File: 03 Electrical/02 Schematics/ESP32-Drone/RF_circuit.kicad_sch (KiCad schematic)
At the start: 0 parts

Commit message: started placing the esp32 circuitry
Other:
- note added: "Determine the LoRA module that we will use"
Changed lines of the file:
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@@
 	(generator_version "9.0")
 	(paper "A4")
+	(text "Determine the LoRA module that we will use \n"
+		(exclude_from_sim no)
+		(at 51.308 48.768 0)
+		(effects
+			(font
+				(size 1.27 1.27)
+			)
+		)
+	)
 )

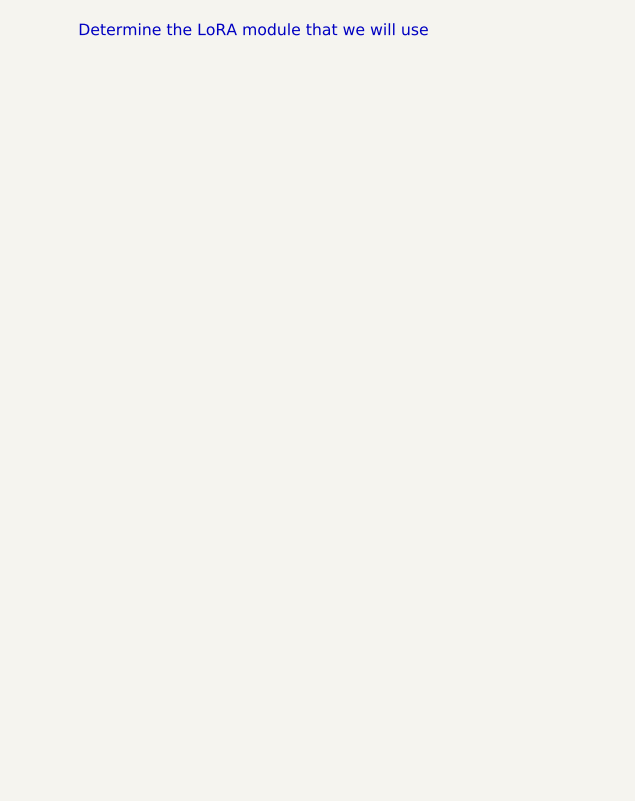
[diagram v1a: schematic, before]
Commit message: added the communication module
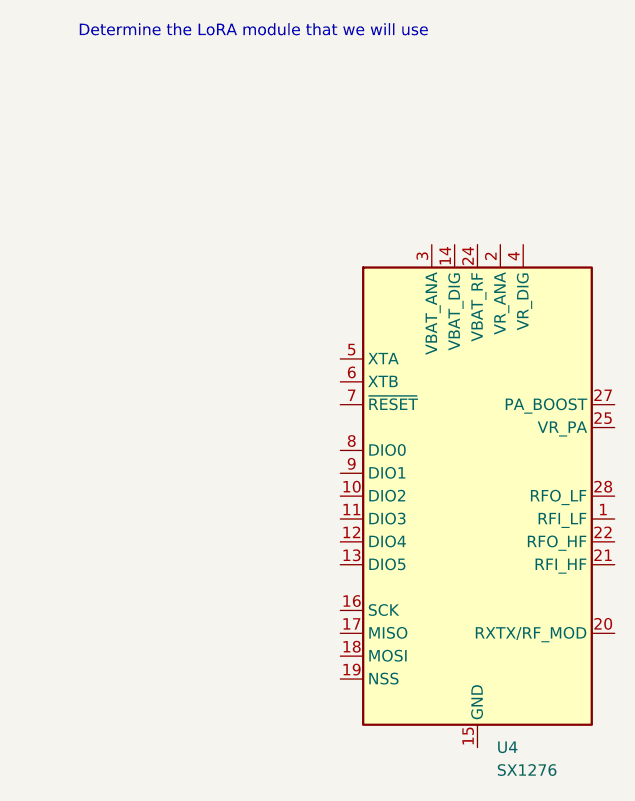
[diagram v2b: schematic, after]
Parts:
- added U4: SX1276, Package_DFN_QFN:QFN-28-1EP_6x6mm_P0.65mm_EP4.8x4.8mm, symbol RF:SX1276
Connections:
- new net: U4.15 (GND), U4.23 (GND), U4.26 (GND), U4.29 (GND)
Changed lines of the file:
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@@
+		)
+	)
+	(symbol
+		(lib_id "RF:SX1276")
+		(at 76.2 100.33 0)
+		(unit 1)
+		(exclude_from_sim no)
+		(in_bom yes)
+		(on_board yes)
+		(dnp no)
+		(fields_autoplaced yes)
+		(property "Reference" "U4"
+			(at 78.3433 128.27 0)
+			(effects
+				(font
+					(size 1.27 1.27)
+				)
+				(justify left)
+			)
+		)
+		(property "Value" "SX1276"
+			(at 78.3433 130.81 0)
+			(effects
+				(font
+					(size 1.27 1.27)
+				)
+				(justify left)
+			)
+		)
+		(property "Footprint" "Package_DFN_QFN:QFN-28-1EP_6x6mm_P0.65mm_EP4.8x4.8mm"
+			(at 76.2 107.95 0)
+			(effects
+				(font
+					(size 1.27 1.27)
+				)
+				(hide yes)
+			)
+		)
+		(property "Datasheet" "https://semtech.my.salesforce.com/sfc/p/#E0000000JelG/a/2R0000001Rbr/6EfVZUorrpoKFfvaF_Fkpgp5kzjiNyiAbqcpqh9qSjE"
+			(at 76.2 105.41 0)
+			(effects
+				(font
+					(size 1.27 1.27)
+				)
+				(hide yes)
+			)
+		)
+		(property "Description" "137 MHz to 1020 MHz Low Power Long Range Transceiver, spreading factor from 6 to 12, LoRA, QFN-28"
+			(at 76.2 100.33 0)
+			(effects
+				(font
+					(size 1.27 1.27)
+				)
+				(hide yes)
+			)
+		)
+		(pin "9"
+		)
+		(pin "8"
+		)
+		(pin "7"
+		)
+		(pin "6"
+		)
+		(pin "5"
+		)
+		(pin "13"
+		)
+		(pin "11"
+		)
+		(pin "10"
+		)
+		(pin "2"
+		)
+		(pin "4"
+		)
+		(pin "27"
+		)
+		(pin "25"
+		)
+		(pin "16"
+		)
+		(pin "17"
+		)
+		(pin "20"
+		)
+		(pin "28"
+		)
+		(pin "1"
+		)
+		(pin "22"
+		)
+		(pin "21"
+		)
+		(pin "24"
+		)
+		(pin "15"
+		)
+		(pin "23"
+		)
+		(pin "26"
+		)
+		(pin "29"
+		)
+		(pin "18"
+		)
+		(pin "19"
+		)
+		(pin "3"
+		)
+		(pin "14"
+		)
+		(pin "12"
+		)
+		(instances
+			(project ""
+				(path "/2b6165e2-6038-49be-a1b7-174ab2023d42/1dc35de0-9c0f-47b6-8fc2-6b9c6dde3360"
+					(reference "U4")
+					(unit 1)
+				)
+			)
 		)
 	)
